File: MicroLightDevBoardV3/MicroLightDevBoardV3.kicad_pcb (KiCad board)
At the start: 6 copper layers, 12.5 x 18 mm, 34 parts, among them J1 TYPE-C-31-M-12, J3 Conn_01x03_Socket, J4 Conn_01x01_Socket, J5 Conn_01x01_Socket, J6 Conn_01x04_Socket, SW1 SW_Push, U1 USBLC6-2P6, U2 STM32C071GBUx, U3 BQ25180, U4 S-85S1AB33-I6T1U, U5 DF53-2S-0.6H, U7 MC3479

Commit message: rules checker fix
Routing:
- net GND: track 30.4 -> 31.9 mm
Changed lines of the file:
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@@
+	)
+	(segment
+		(start 53.825 31.925)
+		(end 53.6 31.925)
+		(width 0.2)
+		(layer "In1.Cu")
+		(net 2)
+	)
+	(segment
+		(start 54.75 31)
+		(end 53.825 31.925)
+		(width 0.2)
+		(layer "In1.Cu")
+		(net 2)
 	)
 	(segment

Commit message: cleanup traces
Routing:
- net VBUS_CHRG: track 22.0 -> 20.9 mm
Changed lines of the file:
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@@
 	)
 	(segment
-		(start 47.474 23.917479)
-		(end 47.536 23.855479)
+		(start 47.649 24.392479)
+		(end 48.092479 23.949)
+		(width 0.2)
+		(layer "F.Cu")
+		(net 1)
+	)
+	(segment
+		(start 54.851 26.686785)
+		(end 54.851 24.923215)
+		(width 0.2)
+		(layer "F.Cu")
+		(net 1)
+	)
+	(segment
+		(start 48.092479 23.949)
+		(end 50.049 23.949)
+		(width 0.2)
+		(layer "F.Cu")
+		(net 1)
+	)
+	(segment
+		(start 47.3 25.855001)
+		(end 47.649 25.506001)
+		(width 0.2)
+		(layer "F.Cu")
+		(net 1)
+	)
+	(segment
+		(start 47.3 26.58)
+		(end 47.3 25.855001)
 		(width 0.2)
 		(layer "F.Cu")
@@
 	)
 	(segment
-		(start 47.536 26.344)
-		(end 47.536 24.394521)
-		(width 0.2)
-		(layer "F.Cu")
-		(net 1)
-	)
-	(segment
-		(start 51.876 23.567112)
-		(end 51.876 23.051)
-		(width 0.2)
-		(layer "F.Cu")
-		(net 1)
-	)
-	(segment
-		(start 51.876 23.051)
-		(end 51.65 22.825)
-		(width 0.2)
-		(layer "F.Cu")
-		(net 1)
-	)
-	(segment
-		(start 47.536 23.855479)
-		(end 47.536 23.789)
-		(width 0.2)
-		(layer "F.Cu")
-		(net 1)
-	)
-	(segment
-		(start 47.536 24.394521)
-		(end 47.474 24.332521)
-		(width 0.2)
-		(layer "F.Cu")
-		(net 1)
-	)
-	(segment
-		(start 47.75 23.575)
-		(end 49.675 23.575)
-		(width 0.2)
-		(layer "F.Cu")
-		(net 1)
-	)
-	(segment
-		(start 52.376 24.067112)
-		(end 51.876 23.567112)
+		(start 50.9 22.825)
+		(end 50.2 23.525)
+		(width 0.2)
+		(layer "F.Cu")
+		(net 1)
+	)
+	(segment
+		(start 53.318215 27.556)
+		(end 53.718215 27.156)
+		(width 0.2)
+		(layer "F.Cu")
+		(net 1)
+	)
+	(segment
+		(start 47.649 25.506001)
+		(end 47.649 24.392479)
+		(width 0.2)
+		(layer "F.Cu")
+		(net 1)
+	)
+	(segment
+		(start 54.381785 27.156)
+		(end 54.851 26.686785)
+		(width 0.2)
+		(layer "F.Cu")
+		(net 1)
+	)
+	(segment
+		(start 50.049 23.949)
+		(end 50.2 24.1)
+		(width 0.2)
+		(layer "F.Cu")
+		(net 1)
+	)
+	(segment
+		(start 52.2 26.58)
+		(end 52.2 27.304999)
+		(width 0.2)
+		(layer "F.Cu")
+		(net 1)
+	)
+	(segment
+		(start 52.451001 27.556)
+		(end 53.318215 27.556)
+		(width 0.2)
+		(layer "F.Cu")
+		(net 1)
+	)
+	(segment
+		(start 52.2 27.304999)
+		(end 52.451001 27.556)
+		(width 0.2)
+		(layer "F.Cu")
+		(net 1)
+	)
+	(segment
+		(start 53.994897 24.067112)
+		(end 52.767112 24.067112)
 		(width 0.2)
 		(layer "F.Cu")
@@
 	)
 	(segment
-		(start 52.451001 27.556)
-		(end 52.2 27.304999)
-		(width 0.2)
-		(layer "F.Cu")
-		(net 1)
-	)
-	(segment
-		(start 47.474 24.332521)
-		(end 47.474 23.917479)
-		(width 0.2)
-		(layer "F.Cu")
-		(net 1)
-	)
-	(segment
-		(start 50.9 22.825)
-		(end 50.2 23.525)
-		(width 0.2)
-		(layer "F.Cu")
-		(net 1)
-	)
-	(segment
-		(start 53.318215 27.556)
-		(end 52.451001 27.556)
+		(start 51.525 22.825)
+		(end 50.9 22.825)
 		(width 0.2)
 		(layer "F.Cu")
@@
 	)
 	(segment
-		(start 47.3 26.58)
-		(end 47.536 26.344)
-		(width 0.2)
-		(layer "F.Cu")
-		(net 1)
-	)
-	(segment
-		(start 49.675 23.575)
-		(end 50.2 24.1)
-		(width 0.2)
-		(layer "F.Cu")
-		(net 1)
-	)
-	(segment
-		(start 54.851 26.686785)
-		(end 54.851 24.923215)
-		(width 0.2)
-		(layer "F.Cu")
-		(net 1)
-	)
-	(segment
-		(start 47.536 23.789)
-		(end 47.75 23.575)
-		(width 0.2)
-		(layer "F.Cu")
-		(net 1)
-	)
-	(segment
-		(start 54.381785 27.156)
-		(end 54.851 26.686785)
-		(width 0.2)
-		(layer "F.Cu")
-		(net 1)
-	)
-	(segment
-		(start 53.994897 24.067112)
-		(end 52.376 24.067112)
-		(width 0.2)
-		(layer "F.Cu")
-		(net 1)
-	)
-	(segment
-		(start 53.718215 27.156)
-		(end 53.318215 27.556)
-		(width 0.2)
-		(layer "F.Cu")
-		(net 1)
-	)
-	(segment
-		(start 52.2 27.304999)
-		(end 52.2 26.58)
-		(width 0.2)
-		(layer "F.Cu")
-		(net 1)
-	)
-	(segment
-		(start 51.65 22.825)
-		(end 50.9 22.825)
+		(start 52.767112 24.067112)
+		(end 51.525 22.825)
 		(width 0.2)
 		(layer "F.Cu")
@@
 	)
 	(segment
-		(start 48 24.15)
-		(end 47.975 24.125)
+		(start 48.3 24.45)
+		(end 48 24.75)
 		(width 0.2)
 		(layer "F.Cu")
@@
 	)
 	(segment
-		(start 48 26.58)
-		(end 48 24.15)
+		(start 48 24.75)
+		(end 48 26.58)
 		(width 0.2)
 		(layer "F.Cu")
@@
 	)
 	(via
-		(at 47.975 24.125)
+		(at 48.3 24.45)
 		(size 0.4)
 		(drill 0.3)
@@
 	(segment
 		(start 46.875 23.025)
-		(end 47.975 24.125)
+		(end 48.3 24.45)
 		(width 0.2)
 		(layer "In2.Cu")
@@
 	)
 	(segment
-		(start 48.864 22.602)
-		(end 48.864 21.689162)
+		(start 47.114 25.956008)
+		(end 47.536 25.534008)
+		(width 0.2)
+		(layer "B.Cu")
+		(net 27)
+	)
+	(segment
+		(start 48.864 22.624372)
+		(end 48.95 22.710372)
+		(width 0.2)
+		(layer "B.Cu")
+		(net 27)
+	)
+	(segment
+		(start 47.8125 27.45)
+		(end 47.429912 27.45)
 		(width 0.2)
 		(layer "B.Cu")
@@
 	)
 	(segment
-		(start 48.891 22.629)
-		(end 48.864 22.602)
+		(start 46.285 28.543612)
+		(end 47.378612 27.45)
+		(width 0.2)
+		(layer "B.Cu")
+		(net 27)
+	)
+	(segment
+		(start 48.864 21.689162)
+		(end 48.864 22.624372)
+		(width 0.2)
+		(layer "B.Cu")
+		(net 27)
+	)
+	(segment
+		(start 48.673 23.7425)
+		(end 48.298979 23.7425)
+		(width 0.2)
+		(layer "B.Cu")
+		(net 27)
+	)
+	(segment
+		(start 47.429912 27.45)
+		(end 47.114 27.134088)
 		(width 0.2)
 		(layer "B.Cu")
@@
 	)
 	(segment
+		(start 48.95 23.4655)
+		(end 48.673 23.7425)
+		(width 0.2)
+		(layer "B.Cu")
+		(net 27)
+	)
+	(segment
+		(start 48.864 21.689162)
+		(end 49.428162 21.125)
+		(width 0.2)
+		(layer "B.Cu")
+		(net 27)
+	)
+	(segment
+		(start 48.95 22.710372)
+		(end 48.95 23.4655)
+		(width 0.2)
+		(layer "B.Cu")
+		(net 27)
+	)
+	(segment
 		(start 49.428162 21.125)
 		(end 50.3 21.125)
@@
 	)
 	(segment
-		(start 47.474 23.917479)
-		(end 47.820479 23.571)
+		(start 47.536 24.505479)
+		(end 47.536 25.534008)
 		(width 0.2)
 		(layer "B.Cu")
@@
 	)
 	(segment
-		(start 47.474 24.332521)
-		(end 47.474 23.917479)
-		(width 0.2)
-		(layer "B.Cu")
-		(net 27)
-	)
-	(segment
-		(start 46.285 28.543612)
-		(end 47.378612 27.45)
-		(width 0.2)
-		(layer "B.Cu")
-		(net 27)
-	)
-	(segment
-		(start 48.891 23.348628)
-		(end 48.891 22.629)
-		(width 0.2)
-		(layer "B.Cu")
-		(net 27)
-	)
-	(segment
-		(start 48.668628 23.571)
-		(end 48.891 23.348628)
-		(width 0.2)
-		(layer "B.Cu")
-		(net 27)
-	)
-	(segment
-		(start 47.8125 27.45)
-		(end 47.429912 27.45)
-		(width 0.2)
-		(layer "B.Cu")
-		(net 27)
-	)
-	(segment
-		(start 48.864 21.689162)
-		(end 49.428162 21.125)
-		(width 0.2)
-		(layer "B.Cu")
-		(net 27)
-	)
-	(segment
-		(start 47.536 25.534008)
-		(end 47.536 24.394521)
-		(width 0.2)
-		(layer "B.Cu")
-		(net 27)
-	)
-	(segment
-		(start 47.536 24.394521)
-		(end 47.474 24.332521)
-		(width 0.2)
-		(layer "B.Cu")
-		(net 27)
-	)
-	(segment
-		(start 47.820479 23.571)
-		(end 48.668628 23.571)
-		(width 0.2)
-		(layer "B.Cu")
-		(net 27)
-	)
-	(segment
-		(start 47.429912 27.45)
-		(end 47.114 27.134088)
-		(width 0.2)
-		(layer "B.Cu")
-		(net 27)
-	)
-	(segment
-		(start 47.114 25.956008)
-		(end 47.536 25.534008)
-		(width 0.2)
-		(layer "B.Cu")
+		(start 48.298979 23.7425)
+		(end 47.536 24.505479)
+		(width 0.2)
+		(layer "B.Cu")

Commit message: rename fBlue to fBlueBulb as it controls power for blue in rgb led, as well as power for 2 pin bulb leds
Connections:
- net fBlue renamed fBlueBulb
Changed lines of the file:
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@@
 	(net 52 "fRed")
 	(net 53 "fGreen")
-	(net 54 "fBlue")
+	(net 54 "fBlueBulb")
 	(net 55 "unconnected-(U2-PA5-Pad11)")
 	(footprint "MicroLightDevBoard:PinSocket_1x03_P2.54mm_Vertical_debug"
@@
 			(net 1 "VBUS_CHRG")
 			(pinfunction "VBUS")
-			(pintype "passive")
+			(pintype "power_out")
 		)
 		(pad "A5" smd roundrect
@@
 			(layers "B.Cu" "B.Mask" "B.Paste")
 			(roundrect_rratio 0.25)
-			(net 54 "fBlue")
+			(net 54 "fBlueBulb")
 			(pinfunction "PA8")
 			(pintype "bidirectional")
@@
 			(layers "B.Cu" "B.Mask" "B.Paste")
 			(roundrect_rratio 0.25)
-			(net 54 "fBlue")
+			(net 54 "fBlueBulb")
 			(pintype "passive")
 		)

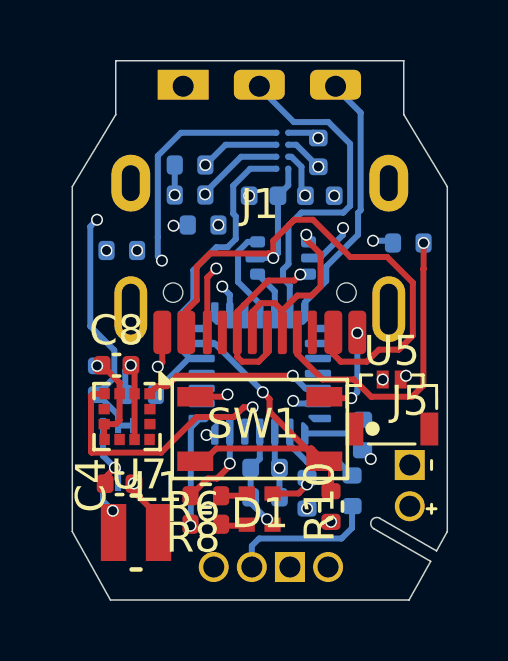
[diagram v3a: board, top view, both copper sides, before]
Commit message: made dev pin area a bit smaller
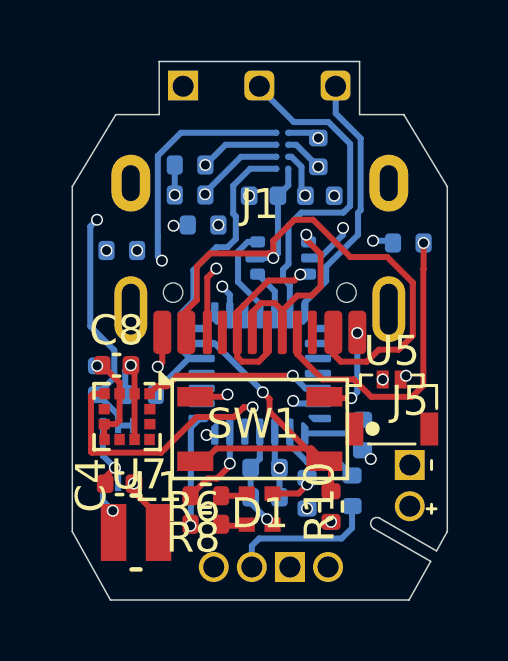
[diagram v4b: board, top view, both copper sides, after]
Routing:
- net GND: track 31.9 -> 28.6 mm
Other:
- board size 12.5 x 18 mm -> 12.5 x 17.9 mm
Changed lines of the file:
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@@
 		(pad "1" thru_hole rect
 			(at 0 0 90)
-			(size 1 1.7)
+			(size 1 1)
 			(drill 0.7
-				(offset 0.05 0)
+				(offset 0.025 0)
 			)
 			(layers "*.Cu" "*.Mask")
@@
 		(pad "2" thru_hole roundrect
 			(at 0 2.54 90)
-			(size 1 1.7)
+			(size 1 1)
 			(drill 0.7
-				(offset 0.05 0)
+				(offset 0.025 0)
 			)
 			(layers "*.Cu" "*.Mask")
@@
 		(pad "3" thru_hole roundrect
 			(at 0 5.08 90)
-			(size 1 1.7)
+			(size 1 1)
 			(drill 0.7
-				(offset 0.05 0)
+				(offset 0.025 0)
 			)
 			(layers "*.Cu" "*.Mask")
@@
 	)
 	(gr_line
+		(start 53.075 19.32)
+		(end 54.55 19.32)
+		(stroke
+			(width 0.05)
+			(type default)
+		)
+		(layer "Edge.Cuts")
+	)
+	(gr_line
+		(start 53.075 17.55)
+		(end 53.075 19.32)
+		(stroke
+			(width 0.05)
+			(type default)
+		)
+		(layer "Edge.Cuts")
+	)
+	(gr_line
 		(start 44.771538 35.5)
 		(end 54.725 35.5)
@@
 	)
 	(gr_line
-		(start 43.5 33.22)
-		(end 44.771538 35.5)
+		(start 53.075 17.55)
+		(end 46.395 17.55)
 		(stroke
 			(width 0.05)
@@
 	)
 	(gr_line
-		(start 44.95 17.525)
-		(end 44.95 19.32)
+		(start 43.5 33.22)
+		(end 44.771538 35.5)
 		(stroke
 			(width 0.05)
@@
 	)
 	(gr_line
-		(start 56 33.22)
-		(end 55.641532 33.86277)
+		(start 46.395 17.55)
+		(end 46.395 19.32)
 		(stroke
 			(width 0.05)
 			(type default)
 		)
-		(locked yes)
 		(layer "Edge.Cuts")
 	)
 	(gr_line
-		(start 54.725 35.5)
-		(end 55.446789 34.21196)
+		(start 56 33.22)
+		(end 55.641532 33.86277)
 		(stroke
 			(width 0.05)
 			(type default)
 		)
+		(locked yes)
 		(layer "Edge.Cuts")
 	)
 	(gr_line
-		(start 54.55 17.525)
-		(end 54.55 19.32)
+		(start 54.725 35.5)
+		(end 55.446789 34.21196)
 		(stroke
 			(width 0.05)
@@
 	)
 	(gr_line
-		(start 53.548207 33.123204)
-		(end 55.446789 34.21196)
+		(start 44.95 19.32)
+		(end 46.395 19.32)
 		(stroke
 			(width 0.05)
 			(type default)
 		)
-		(locked yes)
 		(layer "Edge.Cuts")
 	)
 	(gr_line
-		(start 44.95 17.525)
-		(end 54.55 17.525)
+		(start 53.548207 33.123204)
+		(end 55.446789 34.21196)
 		(stroke
 			(width 0.05)
@@
 	)
 	(segment
-		(start 48.37 19.55)
-		(end 47.195 18.375)
-		(width 0.2)
-		(layer "In1.Cu")
-		(net 2)
-	)
-	(segment
 		(start 53.825 31.925)
 		(end 53.6 31.925)
@@
 	)
 	(segment
-		(start 49.45 19.55)
-		(end 48.37 19.55)
-		(width 0.2)
-		(layer "In1.Cu")
-		(net 2)
-	)
-	(segment
 		(start 54.625 28.075)
 		(end 54.45 28.25)
@@
 	)
 	(segment
-		(start 49.825 19.925)
-		(end 49.45 19.55)
-		(width 0.2)
-		(layer "In1.Cu")
-		(net 2)
-	)
-	(segment
 		(start 50.755 34.4)
 		(end 50.755 33.57)
@@
 	)
 	(segment
-		(start 53.112 22.506226)
-		(end 53.112 19.257)
+		(start 51.25 25.581384)
+		(end 51.964 24.867384)
 		(width 0.2)
 		(layer "B.Cu")
@@
 	)
 	(segment
-		(start 53.025 22.593227)
-		(end 53.112 22.506226)
+		(start 51.25 25.9525)
+		(end 51.25 25.581384)
 		(width 0.2)
 		(layer "B.Cu")
@@
 	)
 	(segment
-		(start 53.025 23.325)
-		(end 53.025 22.593227)
+		(start 51.964 24.386)
+		(end 53.025 23.325)
 		(width 0.2)
 		(layer "B.Cu")
@@
 	)
 	(segment
-		(start 51.964 24.386)
-		(end 53.025 23.325)
+		(start 53.025 22.593227)
+		(end 53.112 22.506226)
 		(width 0.2)
 		(layer "B.Cu")
@@
 	)
 	(segment
-		(start 51.25 25.581384)
-		(end 51.964 24.867384)
+		(start 52.28 19.28)
+		(end 52.28 18.425)
 		(width 0.2)
 		(layer "B.Cu")
@@
 	)
 	(segment
-		(start 53.112 19.257)
-		(end 52.28 18.425)
+		(start 51.964 24.867384)
+		(end 51.964 24.386)
 		(width 0.2)
 		(layer "B.Cu")
@@
 	)
 	(segment
-		(start 51.25 25.9525)
-		(end 51.25 25.581384)
+		(start 53.025 23.325)
+		(end 53.025 22.593227)
 		(width 0.2)
 		(layer "B.Cu")
@@
 	)
 	(segment
-		(start 51.964 24.867384)
-		(end 51.964 24.386)
+		(start 53.112 20.112)
+		(end 52.28 19.28)
+		(width 0.2)
+		(layer "B.Cu")
+		(net 25)
+	)
+	(segment
+		(start 53.112 22.506226)
+		(end 53.112 20.112)
 		(width 0.2)
 		(layer "B.Cu")

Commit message: PCB battery connector, silkscreen, manufacturing changes / Firmware cleanup (#16)
* datasheet misunderstood, charger ic only prevents maximum sys voltage from vin. Using default of 4.5v

* refactor chip_state to move where state is stored. also pass milliseconds in to task instead of calculating and removed associated dependency

* changed error handling in DI layer

* improved labeling on kicad schematic

* update battery connector symbols, attempting to do male connector and wire/crimp assembly

* moved and made battery wire clip slightly smaller

* cleanup and silk screen resizing. Also added James Hunt and v1 silkscreen labels

* add edge cut instructions, add battery connector assembly instructions

* fixing up naming, bom exclusions, made debug pin pad size consistent with other through hole pads

* made debug area a bit smaller at the edges
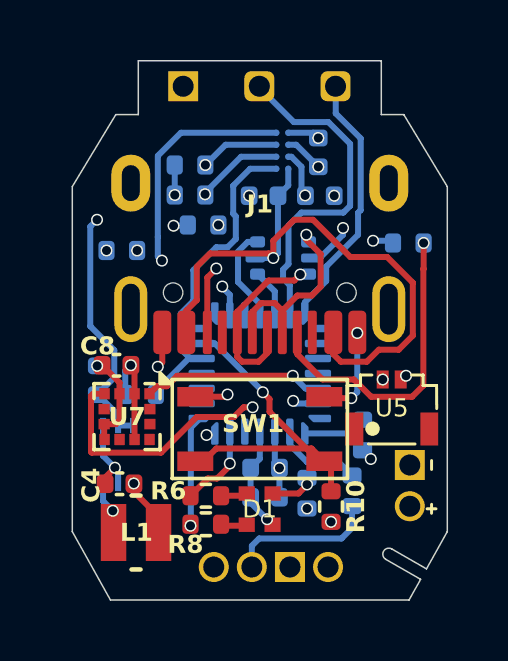
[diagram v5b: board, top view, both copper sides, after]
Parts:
- J3: footprint MicroLightDevBoard:PinSocket_1x03_P2.54mm_Vertical_debug -> MicroLightDevBoard:Microlight_debug_pins
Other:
- board size 12.5 x 17.9 mm -> 12.5 x 18 mm
- board text added: "CLK"
- board text added: "Cut out, no V-cut"
- board text added: "Hunt"
- board text added: "Instructions for battery connector assembly PCB parts: battery connector socket (U6, DF53-2S-0.6H, C31444601) Male Connector parts: battery connector plug (DF53-2P-0.6C, C29857974) battery connector wire crimp (DF53-32PCF, C27763747) black wire (10064-32-1-0500-001-1-TS, C17960034) red wire (10064-32-1-0500-004-1-TS, C17725087) Battery connector must be assembled and attached to battery connector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"
- board text added: "James"
- board text added: "v1"

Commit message: PCB cleanup and cost reduction (#17)
* deleted battery pcb connector. moved button and case led closer to usb

* cleanup wires and gnd plane, remove more connector stuff

* redid battery connection to have wires go through holes on board

* cleanup pcb connections

* minor adjustments to pcb battery wire setup

* silkscreen cleanup and use rounded rect instead of circle for throughhole pads

* cleanup pcb wiring

* cleanup pcb wiring
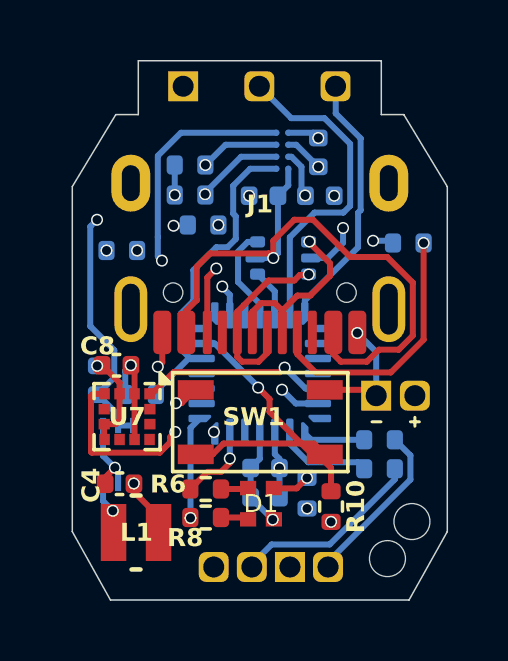
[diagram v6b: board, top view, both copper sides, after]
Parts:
- removed U5: DF53-2S-0.6H, MicroLightDevBoard:DF53-2S-0.6H
- added REF**: wire_hole, MicroLightDevBoard:wire_hole, F.Cu at (54.8, 32.9)
- added REF**: wire_hole, MicroLightDevBoard:wire_hole, F.Cu at (54.0, 34.1)
- moved J4 3.69 mm to (54.9, 28.7), turned to -90 degrees
- moved J5 2.57 mm to (53.6, 28.7)
- moved R12 1.17 mm to (53.7, 31.1), turned to 0 degrees
- moved R11 0.59 mm to (53.7, 30.2), turned to 0 degrees
- moved SW1 0.23 mm to (49.8, 29.6)
- moved R8 0.23 mm to (47.9, 32.8)
- moved R6 0.23 mm to (47.9, 31.8)
- moved D1 0.19 mm to (49.8, 32.3)
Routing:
- net BAT_CHRG: track 15.0 -> 10.7 mm, vias 2 -> 1
- net Net-(J1-CC1): track 10.4 -> 8.86 mm
- net Net-(J6-Pin_2): track 5.02 -> 6.38 mm
- net Net-(J6-Pin_4): track 4.59 -> 5.59 mm, vias 1 -> 0
- net GND: track 28.6 -> 28.5 mm, vias 14 -> 12
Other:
- outline, holes or cut-outs redrawn
- board text removed: "Instructions for battery connector assembly PCB parts: battery connector socket (U6, DF53-2S-0.6H, C31444601) Male Connector parts: battery connector plug (DF53-2P-0.6C, C29857974) battery connector wire crimp (DF53-32PCF, C27763747) black wire (10064-32-1-0500-001-1-TS, C17960034) red wire (10064-32-1-0500-004-1-TS, C17725087) Battery connector must be assembled and attached to battery connector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"

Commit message: Shortern pcb (#18)
* move accelerometer and inductor

* move case led off to side

* shorten pcb by moving resistors, accelerometer, fRGB LED slightly

* rotate battery terminals

* cleanup, silkscreen

* remove more pcb at back

* move chargerIC down

* silkscreen

* silkscreen

* made pcb smaller around usb

* improve front led pads

* cleanup pcb

* commit missed file

* add LCSC part numbers to schematic/pcb

* moved charger ic closer in

* silkscreen
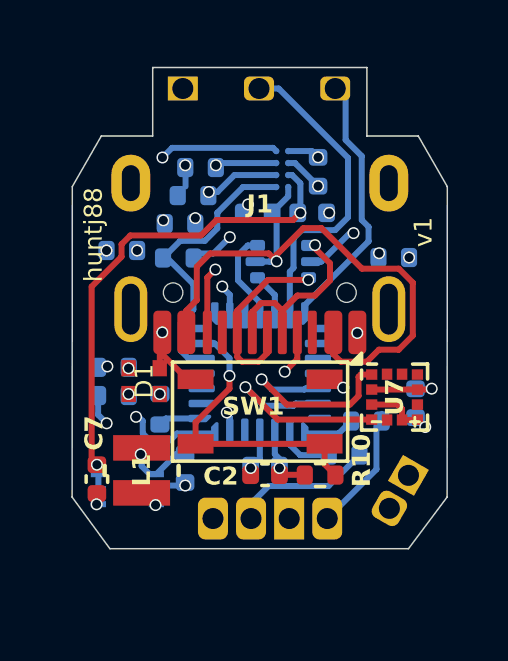
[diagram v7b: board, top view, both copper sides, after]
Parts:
- removed REF** (x2): wire_hole, MicroLightDevBoard:wire_hole
- C2, C7: moved to F.Cu
- C4, C8, R6, R8: moved to B.Cu
- J6: footprint Connector_PinSocket_1.27mm:PinSocket_1x04_P1.27mm_Vertical -> MicroLightDevBoard:rgbLed4Pin_1.27mm
- moved C8 10.0 mm to (54.9, 28.9), turned to 90 degrees
- moved U7 8.94 mm to (54.2, 28.7), turned to 0 degrees
- moved R7 7.70 mm to (44.9, 27.7), turned to 180 degrees
- moved D1 5.64 mm to (45.9, 28.2), turned to 180 degrees
- moved R9 4.72 mm to (47.0, 24.1), turned to 180 degrees
- moved R6 4.38 mm to (44.9, 28.7)
- moved R8 3.92 mm to (46.4, 29.1), turned to -90 degrees
- moved J4 3.85 mm to (54.1, 32.4), turned to 150 degrees
- moved C7 3.30 mm to (44.3, 31.5), turned to -90 degrees
- moved J5 2.86 mm to (54.7, 31.3), turned to -120 degrees
- moved C4 2.25 mm to (47.3, 31.1), turned to -90 degrees
- moved L1 2.08 mm to (45.8, 31.2), turned to -90 degrees
- moved J6 1.62 mm to (48.2, 32.8)
- moved R12 1.26 mm to (52.6, 30.7)
- moved U4 1.20 mm to (45.3, 31.8), turned to 180 degrees
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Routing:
- net GND: track 28.5 -> 19.4 mm, vias 12 -> 13
- net BAT_CHRG: track 10.7 -> 15.0 mm
- net I2C_SDA: track 22.7 -> 18.6 mm, vias 3 -> 2
- net red: track 2.72 -> 6.13 mm, vias 1 -> 2
- net SYS_CHRG: track 18.7 -> 16.6 mm
- net blue: track 3.44 -> 1.42 mm, vias 1 -> 0
- net green: track 4.26 -> 5.94 mm
- net Net-(J6-Pin_2): track 6.38 -> 4.78 mm
- net Net-(J6-Pin_4): track 5.59 -> 4.00 mm
- net Net-(J6-Pin_1): track 12.0 -> 13.6 mm
- net INT_CHRG: track 11.0 -> 9.63 mm
- net fGreen: track 3.23 -> 1.88 mm
- net Net-(D1-GA): track 1.29 -> 0.00 mm
- net TS_MR_CHRG: track 25.2 -> 24.1 mm
- net Net-(D1-BA): track 0.89 -> 0.00 mm, vias 0 -> 1
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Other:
- board size 12.5 x 18 mm -> 12.5 x 16 mm
- board text added: "huntj88"
- board text removed: "Hunt"
- board text removed: "James"
